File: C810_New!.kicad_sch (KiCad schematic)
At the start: 114 parts, among them J1 Conn_01x02_Pin, J10 V_High, J11 W_Low, J12 W_High, J13 V_Low, J14 U_Low, J15 5V, J16 3.3V, J17 12V, J18 Screw_Terminal_01x03, J19 24V, J2 Conn_01x04, J20 GND, J21 GND, J22 GND, J23 GND, J3 Conn_ST_STDC14, J4 USB_C_Receptacle_USB2.0_16P, J5 test, J6 U_current, J7 V_current, J8 W_current, J9 U_High, Q1 BSC159N10LSFG, Q2 BSC159N10LSFG, Q3 BSC159N10LSFG, Q4 BSC159N10LSFG, Q5 BSC159N10LSFG, Q6 BSC159N10LSFG, SW1 Reset, U1 IR2302, U10 L7812, U11 Regulator_3.3, U12 Regulator_5.0, U2 IR2302, U3 IR2302, U4 STM32F303K8Tx, U5 NCS214, U6 NCS214, U7 NCS214, U8 MCP2561-E-SN, Y1 16MHz

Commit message: LowSideでの電流検出に変更
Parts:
- removed J20, J21, J22: GND, Connector_PinHeader_1.00mm:PinHeader_1x01_P1.00mm_Vertical, symbol Connector:Conn_01x01_Pin
- C20: value 2.2μ -> 1μ
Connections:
- net +24V: no longer R13.1, R14.1, R15.1, R16.1, R19.1, R20.1
- net GND: now also R13.2, R14.2, R17.1, R18.1, R19.2, R21.1; no longer D5.2 (A), D6.2 (A), D9.2 (A), Q2.1 (S), Q2.2 (S), Q2.3 (S), Q4.1 (S), Q4.2 (S), Q4.3 (S), Q6.1 (S), Q6.2 (S), Q6.3 (S), R12.2, R3.2, R8.2
- net U_H_Side: no longer R13.2, R17.1
- net V_H_Side: no longer R14.2, R18.1
- net W_H_Side: no longer R19.2, R21.1
- new net U_L_Side: D5.2 (A), Q2.1 (S), Q2.2 (S), Q2.3 (S), R13.1, R16.1, R3.2
- new net V_L_Side: D6.2 (A), Q4.1 (S), Q4.2 (S), Q4.3 (S), R14.1, R15.1, R8.2
- new net W_L_Side: D9.2 (A), Q6.1 (S), Q6.2 (S), Q6.3 (S), R12.2, R19.1, R20.1

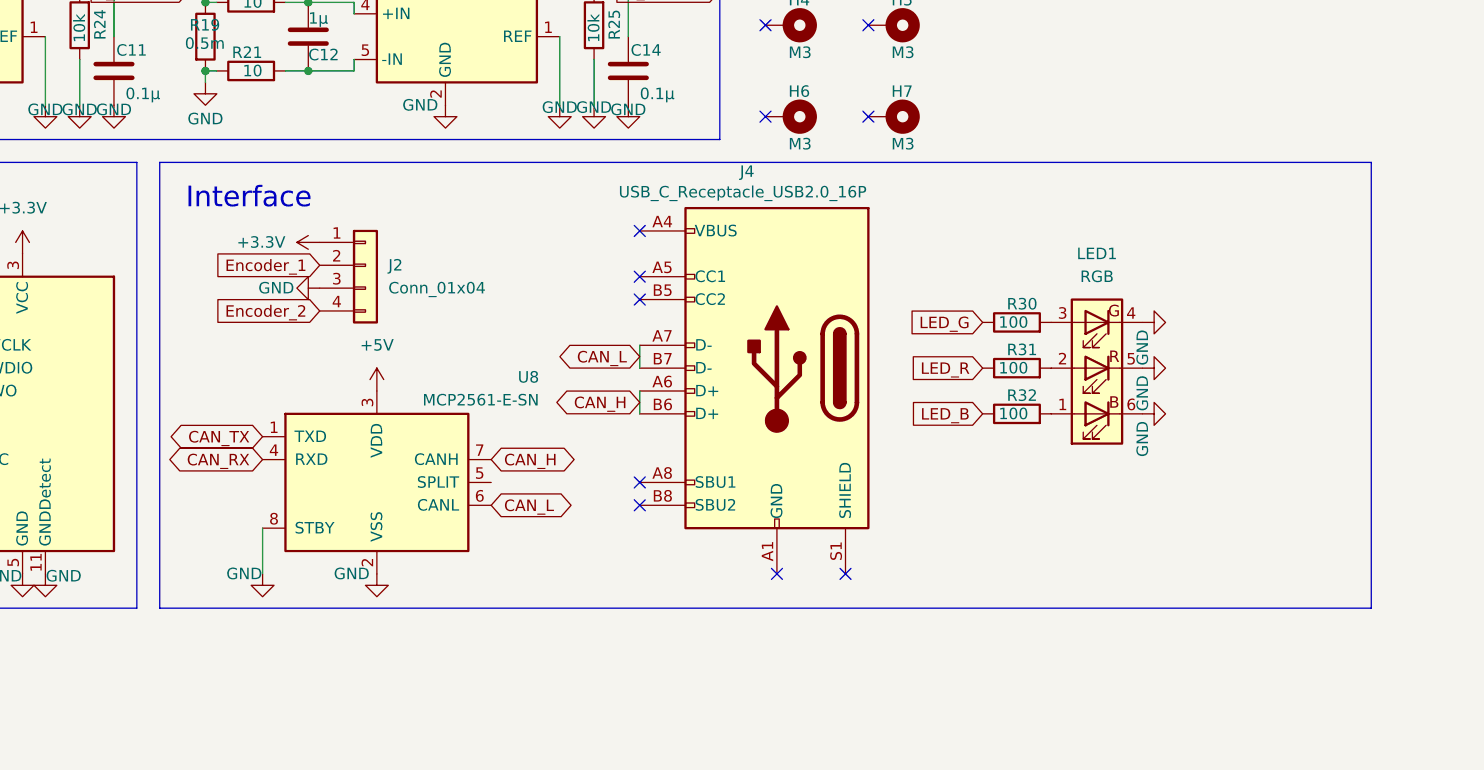
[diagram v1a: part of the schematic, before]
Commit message: M3508用のGHコネクタを追加
PCBの配線し直し開始
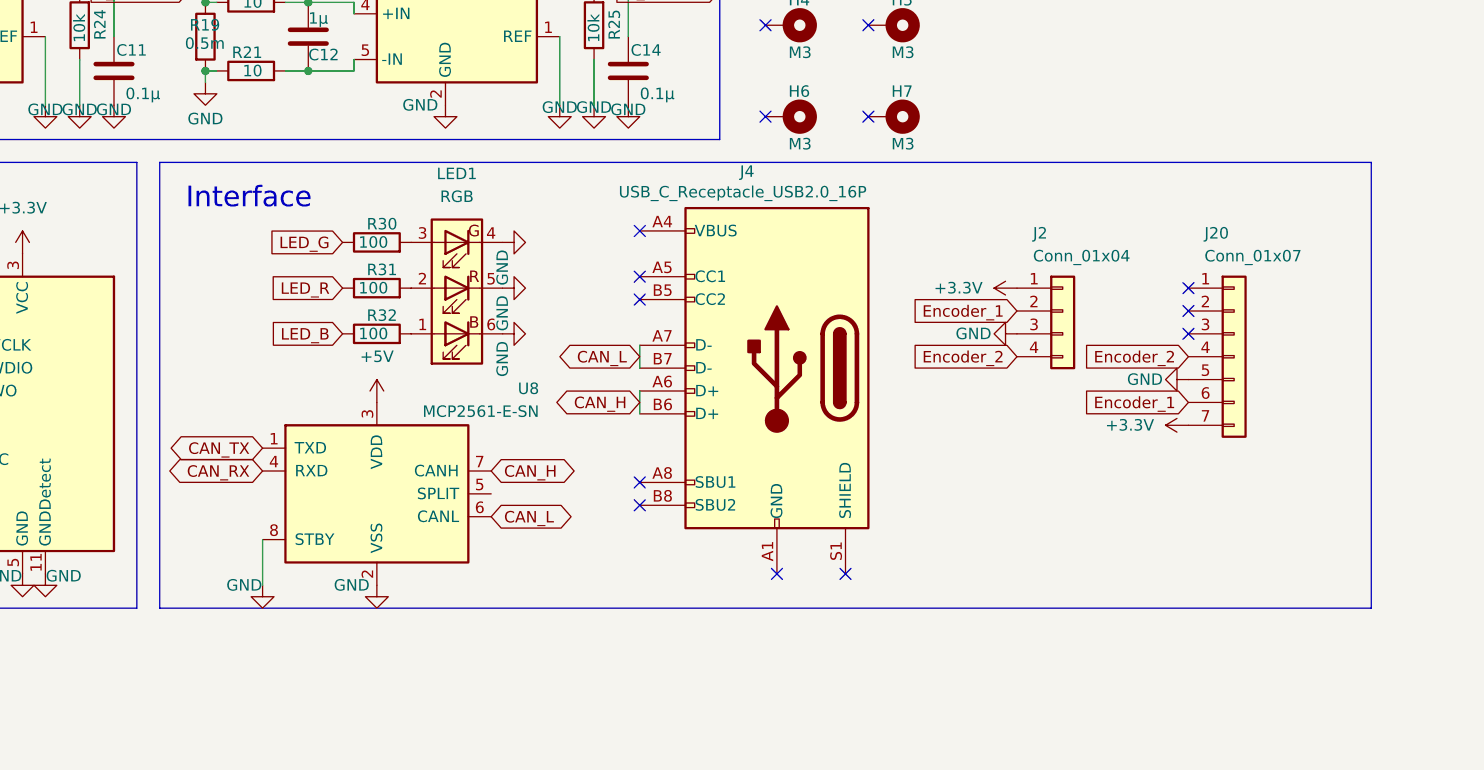
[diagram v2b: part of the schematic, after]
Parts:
- added J20: Conn_01x07, Connector_JST:JST_GH_SM07B-GHS-TB_1x07-1MP_P1.25mm_Horizontal, symbol Connector_Generic:Conn_01x07
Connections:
- net +3.3V: now also J20.7 (Pin_7)
- net Encoder_1: now also J20.6 (Pin_6)
- net Encoder_2: now also J20.4 (Pin_4)
- net GND: now also J20.5 (Pin_5)
- no-connect marks 15 -> 18
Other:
- moved on the sheet: J2, LED1, R30, R31, R32, U8

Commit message: 配線全削除
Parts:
- removed J10: V_High, Connector_PinHeader_1.00mm:PinHeader_1x01_P1.00mm_Vertical, symbol Connector:Conn_01x01_Pin
- removed J11: W_Low, Connector_PinHeader_1.00mm:PinHeader_1x01_P1.00mm_Vertical, symbol Connector:Conn_01x01_Pin
- removed J12: W_High, Connector_PinHeader_1.00mm:PinHeader_1x01_P1.00mm_Vertical, symbol Connector:Conn_01x01_Pin
- removed J13: V_Low, Connector_PinHeader_1.00mm:PinHeader_1x01_P1.00mm_Vertical, symbol Connector:Conn_01x01_Pin
- removed J14: U_Low, Connector_PinHeader_1.00mm:PinHeader_1x01_P1.00mm_Vertical, symbol Connector:Conn_01x01_Pin
- removed J15: 5V, Connector_PinHeader_1.00mm:PinHeader_1x01_P1.00mm_Vertical, symbol Connector:Conn_01x01_Pin
- removed J16: 3.3V, Connector_PinHeader_1.00mm:PinHeader_1x01_P1.00mm_Vertical, symbol Connector:Conn_01x01_Pin
- removed J17: 12V, Connector_PinHeader_1.00mm:PinHeader_1x01_P1.00mm_Vertical, symbol Connector:Conn_01x01_Pin
- removed J23: GND, Connector_PinHeader_1.00mm:PinHeader_1x01_P1.00mm_Vertical, symbol Connector:Conn_01x01_Pin
- removed J6: U_current, TestPoint:TestPoint_Pad_D1.5mm, symbol Connector:Conn_01x01_Pin
- removed J7: V_current, TestPoint:TestPoint_Pad_D1.5mm, symbol Connector:Conn_01x01_Pin
- removed J8: W_current, TestPoint:TestPoint_Pad_D1.5mm, symbol Connector:Conn_01x01_Pin
- removed J9: U_High, Connector_PinHeader_1.00mm:PinHeader_1x01_P1.00mm_Vertical, symbol Connector:Conn_01x01_Pin
- added R33: 10k, Resistor_SMD:R_0603_1608Metric, symbol Device:R
- J5: footprint Connector_PinHeader_1.00mm:PinHeader_1x01_P1.00mm_Vertical -> Connector_PinHeader_2.54mm:PinHeader_1x01_P2.54mm_Vertical
- SW1: value Reset -> button
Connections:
- net +3.3V: now also SW1.2
- net GND: now also R33.2; no longer SW1.1
- net NRST: no longer SW1.2
- net at U4.25 (PA15): now also SW1.1, R33.1
- no-connect marks 18 -> 17
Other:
- moved on the sheet: J2, J20, J3, J4, LED1, R30, R31, R32, SW1, U8

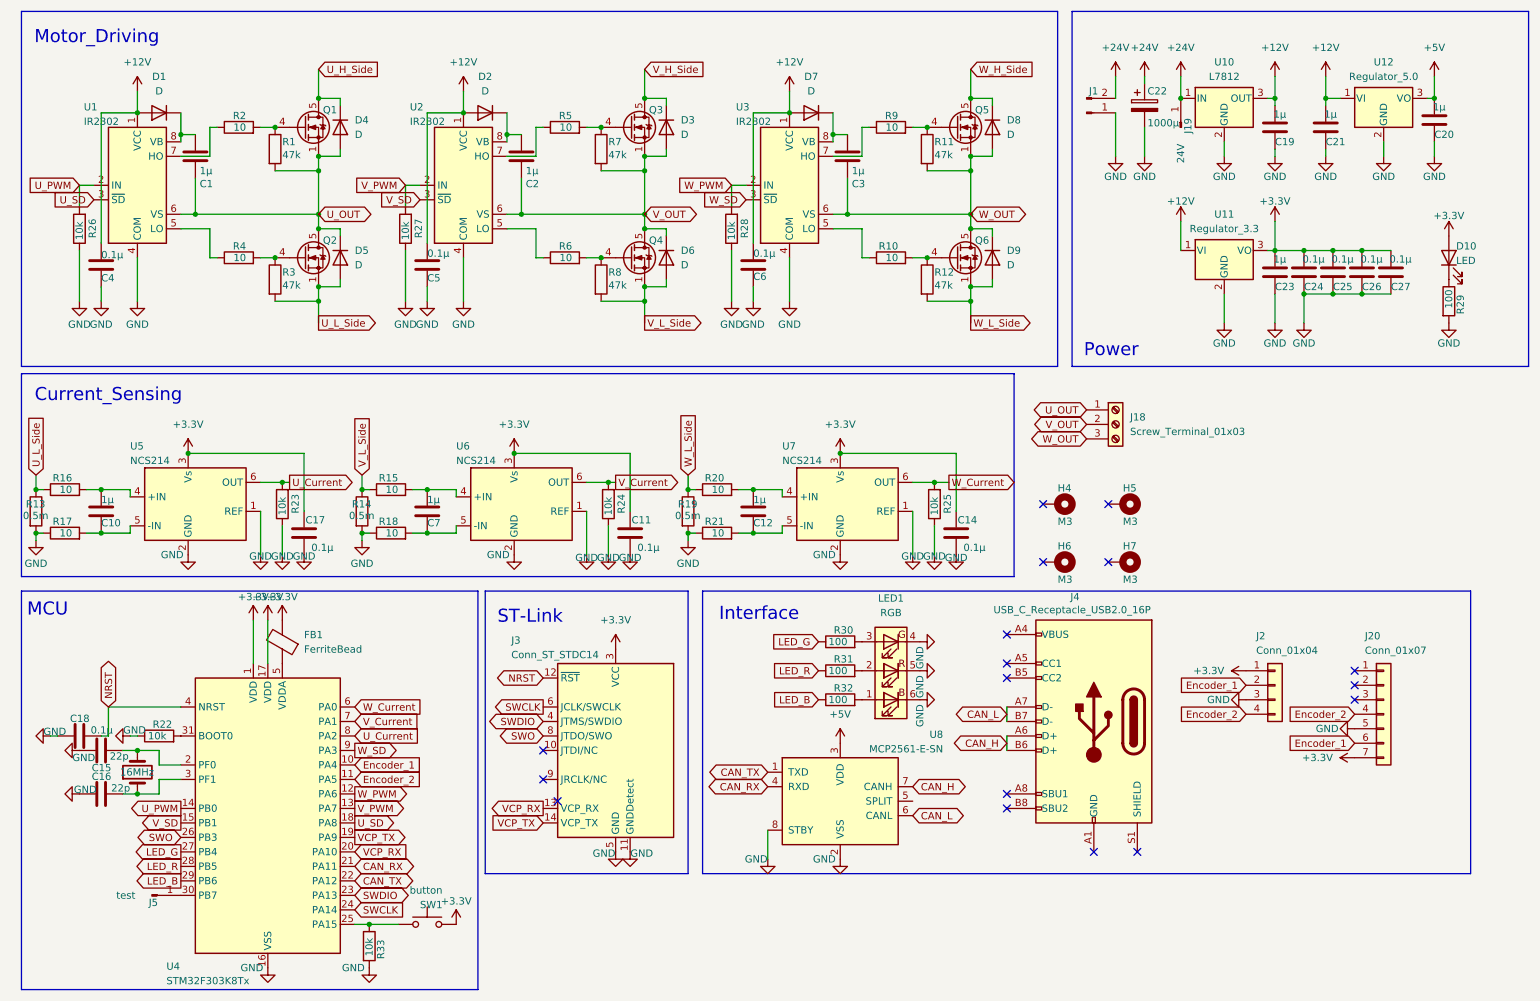
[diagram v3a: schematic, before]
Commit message: C610と同じサイズは無理すぎ
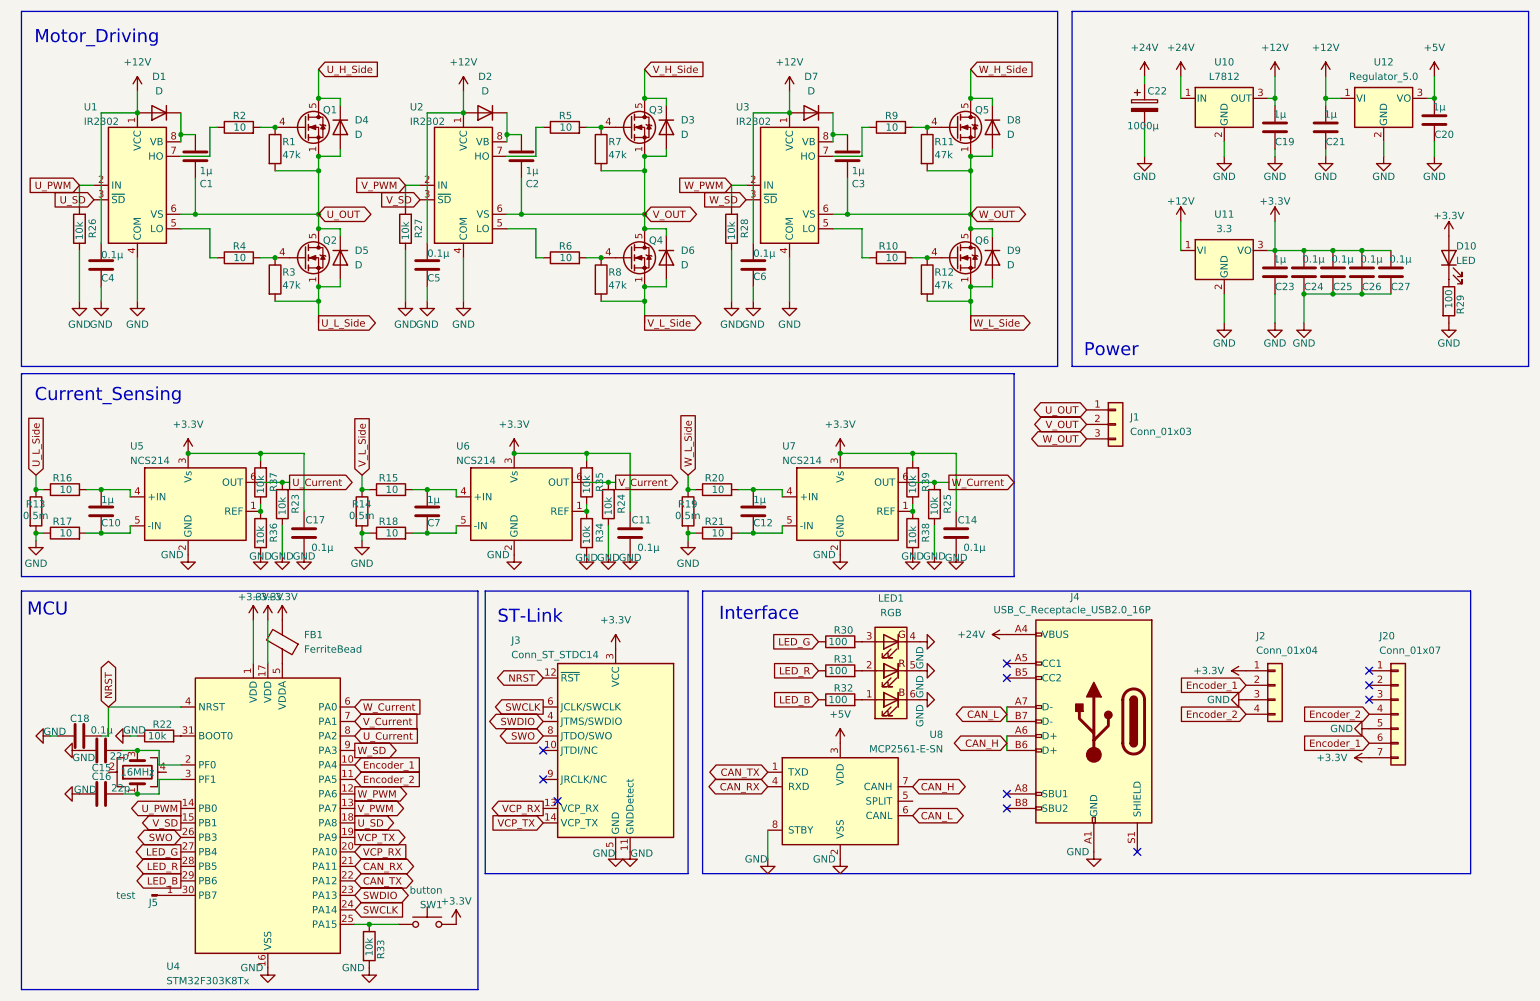
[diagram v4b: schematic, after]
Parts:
- removed H4, H5, H6, H7: M3, MountingHole:MountingHole_3.2mm_M3_Pad_Via, symbol Mechanical:MountingHole_Pad
- removed J1: Conn_01x02_Pin, Connector_AMASS:AMASS_XT60PW-M_1x02_P7.20mm_Horizontal, symbol Connector:Conn_01x02_Pin
- removed J18: Screw_Terminal_01x03, TerminalBlock:TerminalBlock_bornier-3_P5.08mm, symbol Connector:Screw_Terminal_01x03
- removed J19: 24V, Connector_PinHeader_1.00mm:PinHeader_1x01_P1.00mm_Vertical, symbol Connector:Conn_01x01_Pin
- removed Y1: 16MHz, Crystal:Crystal_HC18-U_Vertical, symbol Device:Crystal
- added J1: Conn_01x03, footprints:MR30, symbol Connector_Generic:Conn_01x03
- added R34, R35, R36, R37, R38, R39: 10k, Resistor_SMD:R_0603_1608Metric, symbol Device:R
- added Y2: 16MHz, Crystal:Crystal_SMD_3225-4Pin_3.2x2.5mm_HandSoldering, symbol Device:Crystal_GND24
- U11: value Regulator_3.3 -> 3.3
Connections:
- net +24V: now also J4.A4 (VBUS), J4.A9 (VBUS), J4.B4 (VBUS), J4.B9 (VBUS)
- net +3.3V: now also R35.2, R37.2, R39.2
- net GND: now also J4.A1 (GND), J4.A12 (GND), J4.B1 (GND), J4.B12 (GND), R34.1, R36.1, R38.1; no longer U5.1 (REF), U6.1 (REF), U7.1 (REF)
- net U_OUT: now also J1.1 (Pin_1)
- net V_OUT: now also J1.2 (Pin_2)
- net W_OUT: now also J1.3 (Pin_3)
- net at C15.2, U4.2 (PF0): now also Y2.3
- net at C16.2, U4.3 (PF1): now also Y2.1
- new net: R34.2, R35.1, U6.1 (REF)
- new net: R38.2, R39.1, U7.1 (REF)
- new net: R36.2, R37.1, U5.1 (REF)
- no-connect marks 17 -> 11
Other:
- moved on the sheet: J20

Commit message: あたおかレイアウトを考えてる
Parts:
- removed C10, C12, C7: 1μ, Capacitor_SMD:C_0603_1608Metric, symbol Device:C
- removed C14: 0.1μ, Capacitor_SMD:C_0603_1608Metric_Pad1.08x0.95mm_HandSolder, symbol Device:C
- removed J5: test, Connector_PinHeader_2.54mm:PinHeader_1x01_P2.54mm_Vertical, symbol Connector:Conn_01x01_Pin
- removed R15, R16, R17, R18, R20, R21: 10, Resistor_SMD:R_0603_1608Metric, symbol Device:R
- removed R19: 0.5m, Resistor_SMD:R_2512_6332Metric, symbol Device:R
- removed R23, R24, R25, R26, R27, R28, R38, R39: 10k, Resistor_SMD:R_0603_1608Metric, symbol Device:R
- removed U7: NCS214, Package_TO_SOT_SMD:SOT-363_SC-70-6_Handsoldering, symbol Amplifier_Current:NCS214
- C11, C17: footprint Capacitor_SMD:C_0603_1608Metric_Pad1.08x0.95mm_HandSolder -> Capacitor_SMD:C_0603_1608Metric
- C22: footprint Capacitor_THT:CP_Radial_D12.5mm_P5.00mm -> Capacitor_SMD:CP_Elec_6.3x7.7
- SW1: footprint Button_Switch_THT:SW_PUSH_1P1T_6x3.5mm_H5.0_APEM_MJTP1250 -> Button_Switch_SMD:SW_Push_1P1T_NO_Vertical_Wuerth_434133025816
- Y2: footprint Crystal:Crystal_SMD_3225-4Pin_3.2x2.5mm_HandSoldering -> Crystal:Crystal_SMD_3225-4Pin_3.2x2.5mm
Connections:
- net U_H_Side is gone; now on net +24V: D4.1 (K), Q1.5 (D)
- net V_H_Side is gone; now on net +24V: D3.1 (K), Q3.5 (D)
- net W_H_Side is gone; now on net +24V: D8.1 (K), Q5.5 (D)
- net W_L_Side is gone; now on net GND: D9.2 (A), Q6.1 (S), Q6.2 (S), Q6.3 (S), R12.2
- net GND: now also U5.5 (-IN), U6.5 (-IN)
- net U_L_Side: now also U5.4 (+IN)
- net V_L_Side: now also U6.4 (+IN)
- net W_Current: no longer names the net of U4.6 (PA0)
- no-connect marks 11 -> 13
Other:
- moved on the sheet: J1

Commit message: 配線が無理すぎるので寝る
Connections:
- net Encoder_1: now also U4.11 (PA5); no longer U4.10 (PA4)
- net Encoder_2: now also U4.10 (PA4); no longer U4.11 (PA5)
- net U_Current: now also U4.7 (PA1); no longer U4.8 (PA2)
- net V_Current: now also U4.8 (PA2); no longer U4.7 (PA1)

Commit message: 配線完了
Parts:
- removed D10: LED, LED_SMD:LED_0603_1608Metric_Pad1.05x0.95mm_HandSolder, symbol Device:LED
- removed R29: 100, Resistor_SMD:R_0603_1608Metric, symbol Device:R
